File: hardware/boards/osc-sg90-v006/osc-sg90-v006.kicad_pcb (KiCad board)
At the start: 4 copper layers, 12.1 x 9.6 mm, 34 parts, among them J1 Servo Input, J2 Motor, J3 Debug, J4 Potentiometer, U1 H7133-1_C277537, U4 DRV8837, U5 CH32V006F8U6, U6 74LVC2G241GS,115, U7 ECC204-MAVCZ-T

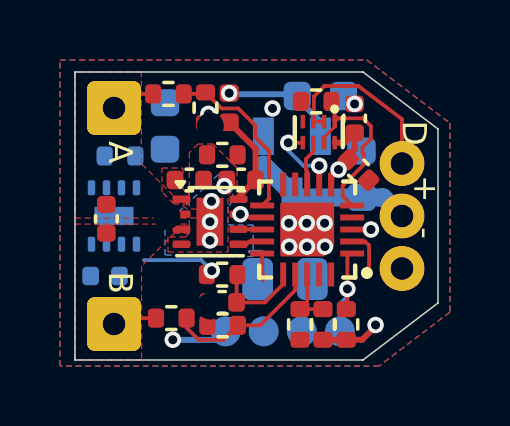
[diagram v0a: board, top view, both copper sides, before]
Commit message: feat(sg90): re-route the board after the manual placement pass
Re-routed with FreeRouting 2.2.4 against a .dsn exported from KiCad 10.0.3
with all tracks cleared and the boundary inset 0.20 mm - Specctra has no
per-item board-edge constraint, so the inset plus the router's own class
clearance is the only lever available.

Result, measured with kicad-cli 10.0.3 (--refill-zones):

  89 track segments, 2 vias
  unconnected items  57 -> 33
  DRC errors          9 -> 9
  DRC warnings        7 -> 7

Every one of the 9 remaining errors is a placement defect that predates the
route (TODO.md §10.3); the route closed 24 connections and introduced no
violations of its own.

J4 is why it does not go further. Its shared:Pot_Wire_Pads footprint uses a
KiCad 10 per-layer padstack - a 0.1 mm token pad on F.Cu inside a 0.9 mm
drill, but real 1.8 mm lands on In1.Cu, In2.Cu and B.Cu. KiCad's Specctra
exporter serialises only the F.Cu shape, concludes the pad has no copper,
and emits no (pin ...) at all, just unnamed keepout circles that FreeRouting
does not honour the same way. The router never learns about the back-side
lands and drives /SWDIO, +3V3 and /VSNA straight across them. Across six
routing configurations, EVERY routing-induced DRC violation involved J4 and
nothing else - no other footprint contributed one.

Injecting a correctly-sized padstack and pins into the .dsn does fix the
routing, but FreeRouting 2.2.4 then hangs writing the session file. So the
conflicting copper is pruned after import instead, with the new
hardware/tools/prune_routing_conflicts.py - driven off KiCad's own DRC
report by UUID rather than re-derived geometry, with a --dangling mode for
the stubs a prune pass leaves behind. Those connections are left for hand
routing: a track crossing a plated land is a short, and there is no correct
automatic placement for it.

The remaining 33 connections are not a router-tuning problem. All six
configurations plateaued at the same 24 internal FreeRouting violations,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
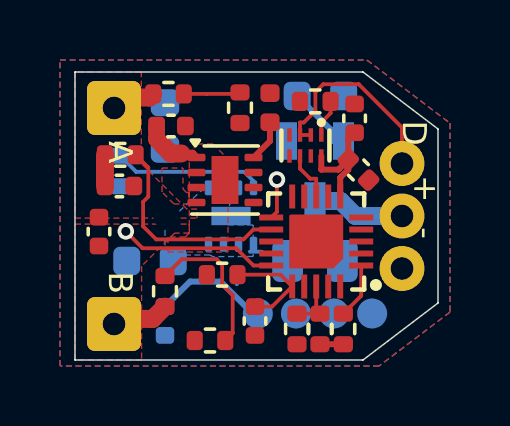
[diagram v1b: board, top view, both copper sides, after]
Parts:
- moved C1 7.62 mm to (102.5, 96.5), turned to 180 degrees
- moved C7 4.06 mm to (101.5, 94.0)
- moved U7 3.90 mm to (105.2, 95.0)
- moved R3 3.40 mm to (101.5, 93.0)
- moved C5 2.50 mm to (103.0, 98.5), turned to -90 degrees
- moved C9 1.90 mm to (103.2, 92.0)
- moved U4 1.48 mm to (105.0, 93.8)
- moved FB1 1.36 mm to (106.5, 91.4)
- moved C6 1.26 mm to (106.0, 98.5), turned to -90 degrees
- moved J3 1.23 mm to (108.0, 98.2)
- moved RS1 1.17 mm to (108.0, 96.5)
- moved R6 1.15 mm to (105.5, 91.4)
- moved R7 0.92 mm to (103.0, 97.5), turned to 90 degrees
- moved U1 0.79 mm to (108.0, 93.5)
- moved R8 0.66 mm to (104.5, 99.2)
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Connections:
- net SE_SWIO renamed /SE_SWIO
- U7 pad 1: (no net) -> unconnected-(U7-NC-Pad1)
- U7 pad 2: (no net) -> unconnected-(U7-NC-Pad2)
- U7 pad 3: (no net) -> unconnected-(U7-NC-Pad3)
- U7 pad 6: (no net) -> unconnected-(U7-NC-Pad6)
- U7 pad 7: (no net) -> unconnected-(U7-NC-Pad7)
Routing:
- net /TX_EN: track 6.29 -> 1.25 mm
- net /SE_SWIO: track 0.00 -> 5.02 mm
- net /SWDIO: track 0.90 -> 5.46 mm, vias 0 -> 1
- net /EN: track 4.00 -> 7.22 mm, vias 1 -> 0
- net /TX: track 2.61 -> 0.00 mm, vias 2 -> 0
- net /VSNA: track 5.81 -> 3.35 mm, vias 0 -> 1
- net /POT: track 2.41 -> 0.00 mm, vias 1 -> 0
- net /3V3_DRV: track 3.17 -> 1.40 mm
- net /nRST: track 3.50 -> 1.85 mm, vias 1 -> 0
- net /ISNS-: track 1.35 -> 0.00 mm
- net PGND: track 0.00 -> 1.04 mm, vias 4 -> 0
- net /IN2: track 0.83 -> 0.00 mm
- net /IN1: track 0.79 -> 0.00 mm
- net /DATA: track 6.14 -> 6.87 mm
- net /ISNS+: track 0.62 -> 0.00 mm, vias 1 -> 0
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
